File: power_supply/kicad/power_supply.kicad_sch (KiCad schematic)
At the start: 19 parts, among them J1 pcie_98, J2 Conn_01x05_Socket, U1 URB2405YMD-10WR3, U2 ESD5344D

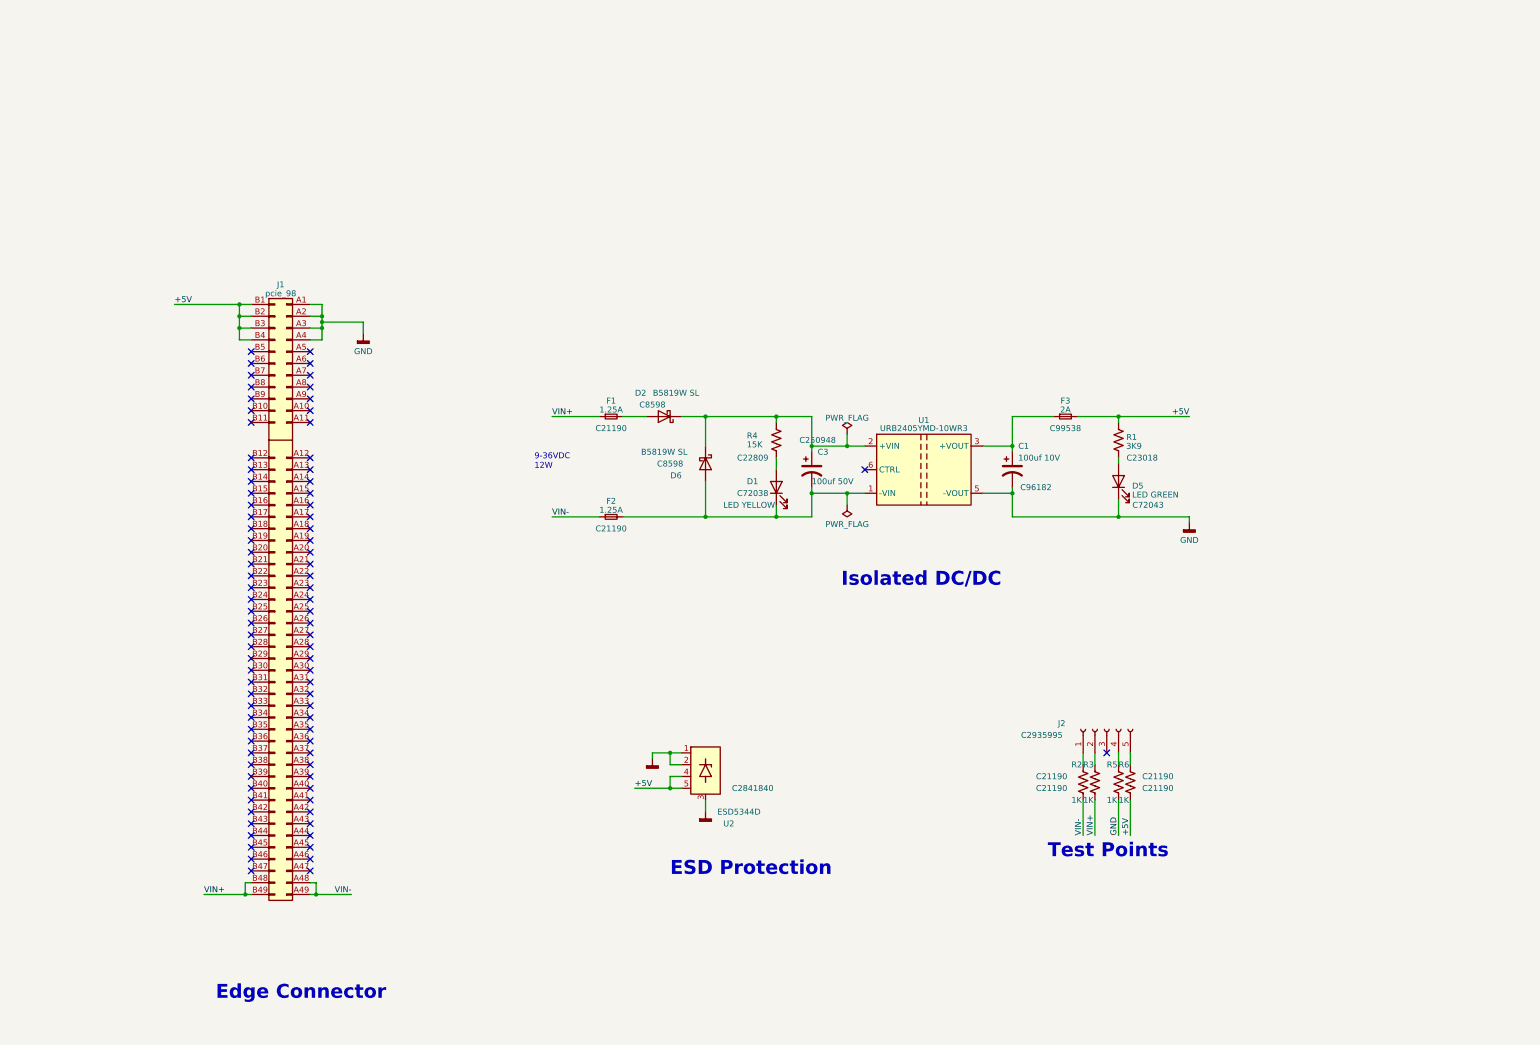
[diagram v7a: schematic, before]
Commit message: Changed the power supply board to use common symbol and footprints from 'common'.
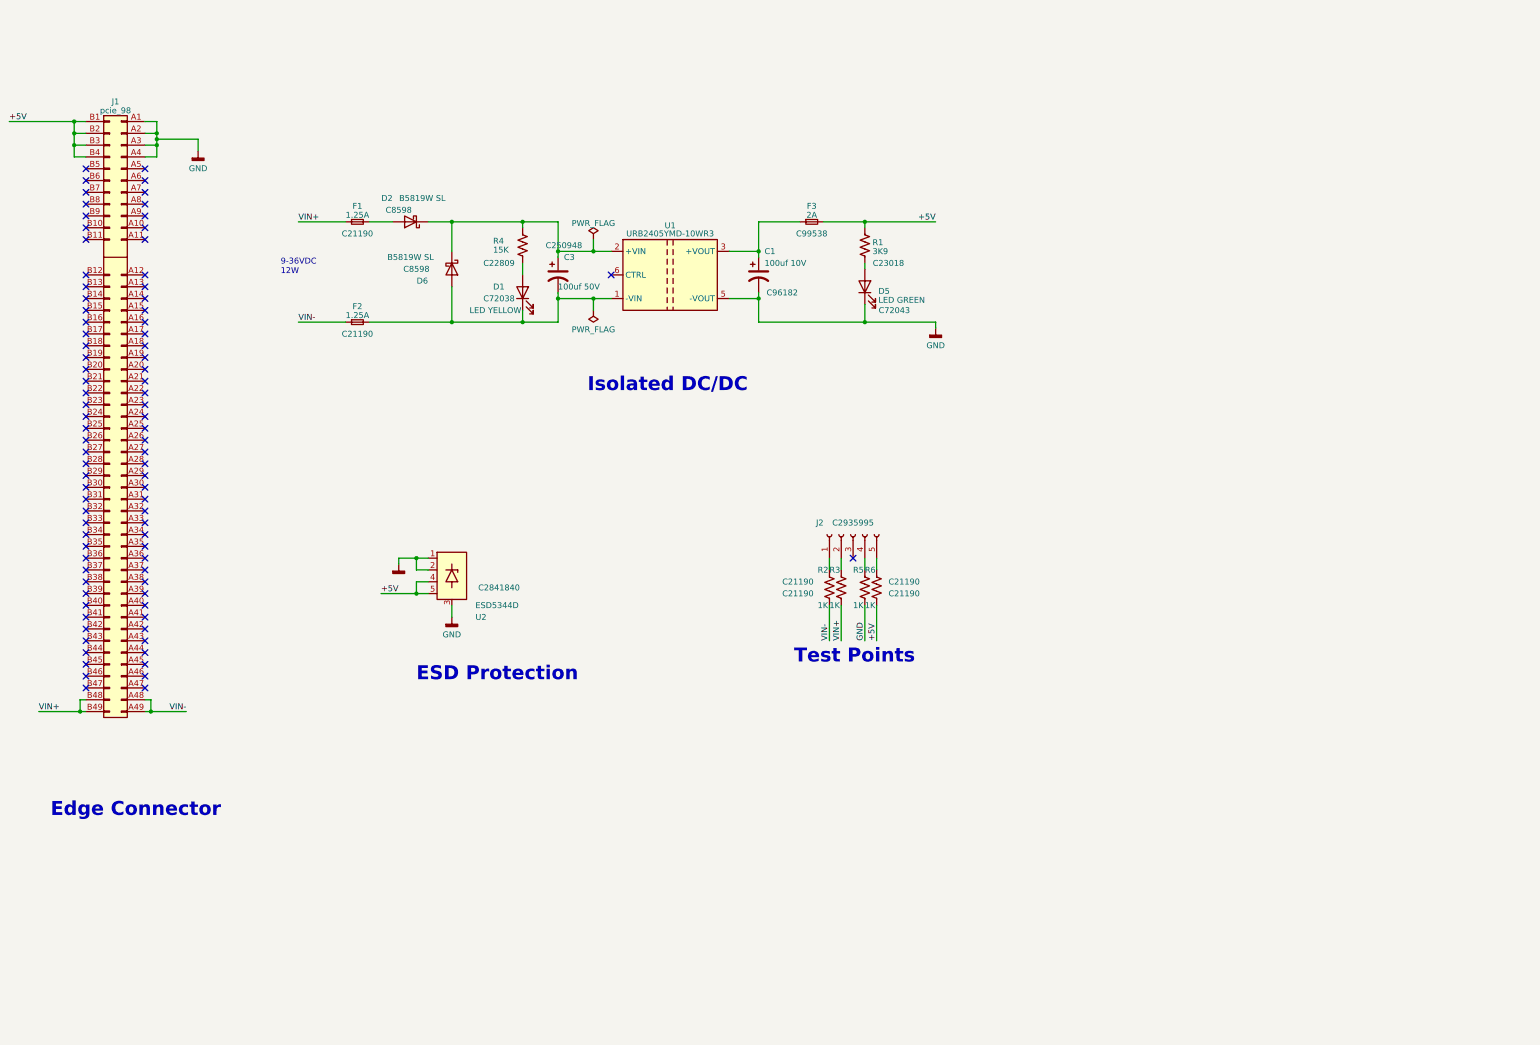
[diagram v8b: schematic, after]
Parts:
- J1: footprint power_supply:pcie_98_edge -> common:PCIE_98_CARD; symbol power_supply:pcie_98 -> common:PCIE_98_EDGE; now in the parts list
- J2: footprint power_supply:PinSocket_1x05_P2.54mm_Horizontal -> common:PinSocket_1x05_P2.54mm_Horizontal_JLCPCB
- U2: footprint power_supply:Diodes_UDFN-10_1.0x2.5mm_P0.5mm -> common:Diodes_UDFN-10_1.0x2.5mm_P0.5mm; symbol power_supply:ESD5344D -> common:ESD5344D
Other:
- moved on the sheet: C1, C3, D1, D2, D5, D6, F1, F2, F3, J1, J2, R1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
